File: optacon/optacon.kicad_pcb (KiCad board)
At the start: 2 copper layers, 61.9 x 95.9 mm, 27 parts, among them J1 Conn_01x12, U1 HV528, U2 HV528, U3 DRV2665

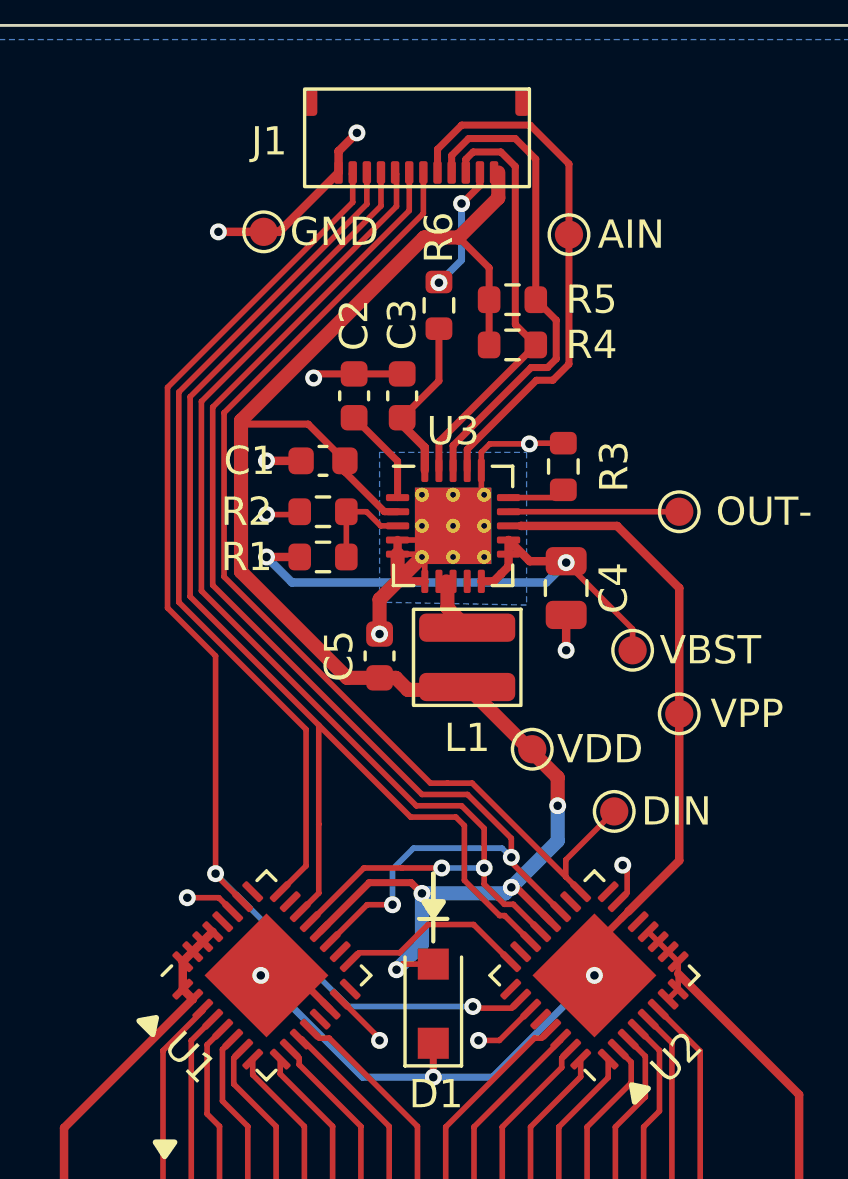
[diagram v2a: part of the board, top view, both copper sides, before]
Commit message: move vias out of pad ; fix ground plane under hv528
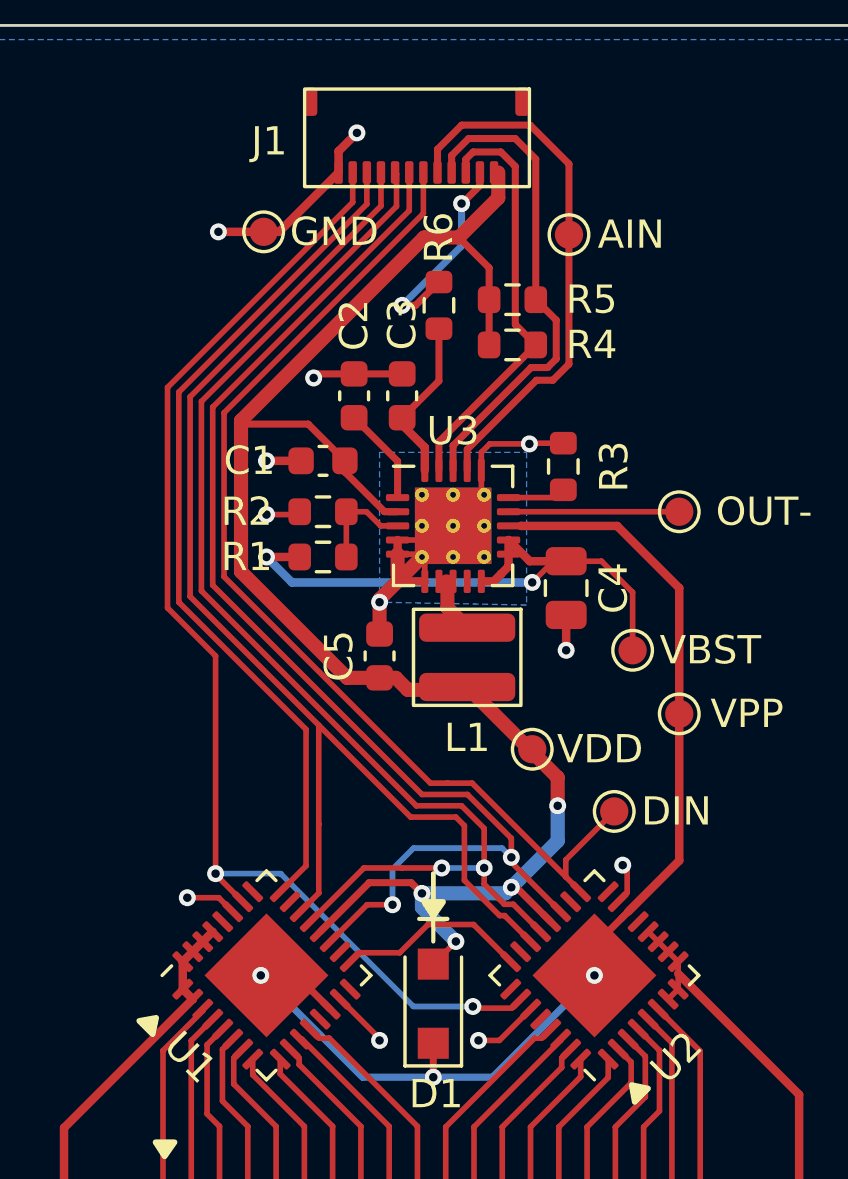
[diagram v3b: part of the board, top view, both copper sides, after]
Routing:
- net /REG: track 4.53 -> 7.49 mm
- net /VDD: track 62.9 -> 61.8 mm
- net /VBST: track 21.0 -> 21.8 mm
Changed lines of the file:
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@@
     )
   )
+  (gr_rect (start 117.4 42.65) (end 90.6 47.75) (layer "B.SilkS") (width 0.15) (fill solid))
   (gr_line (start 103.7 72) (end 104.7 72) (layer "F.SilkS") (width 0.15))
   (gr_poly
@@
   (segment (start 103.3 63.9) (end 105.3 63.9) (width 0.5) (layer "F.Cu") (net 33))
   (segment (start 106.175 50.1) (end 106.175 48.975) (width 0.25) (layer "F.Cu") (net 33))
-  (segment (start 103.098511 73.6) (end 102.9 73.798511) (width 0.2) (layer "F.Cu") (net 33))
   (segment (start 102.3 63.475) (end 102.875 63.475) (width 0.5) (layer "F.Cu") (net 33))
   (segment (start 105.4 63.8) (end 108.6 67) (width 0.5) (layer "F.Cu") (net 33))
@@
   (segment (start 97.4 54.377126) (end 103.877126 47.9) (width 0.5) (layer "F.Cu") (net 33))
   (segment (start 102.477672 57.6) (end 102.9375 57.6) (width 0.25) (layer "F.Cu") (net 33))
+  (segment (start 104.2 73.6) (end 105 72.8) (width 0.2) (layer "F.Cu") (net 33))
   (segment (start 108.353204 72.099651) (end 107.138664 70.885111) (width 0.25) (layer "F.Cu") (net 33))
   (segment (start 106.175 48.975) (end 105.1 47.9) (width 0.25) (layer "F.Cu") (net 33))
@@
   (segment (start 101.075 55.8) (end 99.775 54.5) (width 0.25) (layer "F.Cu") (net 33))
   (segment (start 103.877126 47.9) (end 105.1 47.9) (width 0.5) (layer "F.Cu") (net 33))
-  (segment (start 104.2 73.6) (end 103.098511 73.6) (width 0.2) (layer "F.Cu") (net 33))
   (segment (start 102.3 63.475) (end 101.152126 63.475) (width 0.5) (layer "F.Cu") (net 33))
   (via (at 108.6 68) (size 0.6) (drill 0.3) (layers "F.Cu" "B.Cu") (net 33))
   (via (at 103.8 71.1) (size 0.6) (drill 0.3) (layers "F.Cu" "B.Cu") (net 33))
   (via (at 106.960222 70.884378) (size 0.6) (drill 0.3) (layers "F.Cu" "B.Cu") (net 33))
-  (via (at 102.9 73.798511) (size 0.6) (drill 0.3) (layers "F.Cu" "B.Cu") (net 33))
+  (via (at 105 72.8) (size 0.6) (drill 0.3) (layers "F.Cu" "B.Cu") (net 33))
+  (segment (start 103.8 71.1) (end 103.8 71.6) (width 0.5) (layer "B.Cu") (net 33))
   (segment (start 106.7446 71.1) (end 106.960222 70.884378) (width 0.5) (layer "B.Cu") (net 33))
   (segment (start 103.8 71.1) (end 106.7446 71.1) (width 0.5) (layer "B.Cu") (net 33))
   (segment (start 108.6 68) (end 108.6 69.2446) (width 0.5) (layer "B.Cu") (net 33))
   (segment (start 108.6 69.2446) (end 106.960222 70.884378) (width 0.5) (layer "B.Cu") (net 33))
-  (segment (start 102.9 73.798511) (end 103.8 72.898511) (width 0.5) (layer "B.Cu") (net 33))
-  (segment (start 103.8 72.898511) (end 103.8 71.1) (width 0.5) (layer "B.Cu") (net 33))
+  (segment (start 103.8 71.6) (end 105 72.8) (width 0.5) (layer "B.Cu") (net 33))
   (segment (start 97.460311 71.392544) (end 96.5 70.432233) (width 0.2) (layer "F.Cu") (net 34))
   (segment (start 105.657515 75.157515) (end 105.6 75.1) (width 0.2) (layer "F.Cu") (net 34))
@@
   (segment (start 96.5 62.7) (end 96.5 70.4) (width 0.2) (layer "F.Cu") (net 34))
   (segment (start 107.292544 74.839689) (end 106.974718 75.157515) (width 0.2) (layer "F.Cu") (net 34))
-  (segment (start 101.29952 45.65048) (end 101.35 45.6) (width 0.2) (layer "F.Cu") (net 34))
   (segment (start 106.974718 75.157515) (end 105.657515 75.157515) (width 0.2) (layer "F.Cu") (net 34))
   (via (at 96.5 70.4) (size 0.6) (drill 0.3) (layers "F.Cu" "B.Cu") (net 34))
   (via (at 105.6 75.1) (size 0.6) (drill 0.3) (layers "F.Cu" "B.Cu") (net 34))
-  (segment (start 101.2 75.1) (end 96.5 70.4) (width 0.2) (layer "B.Cu") (net 34))
-  (segment (start 105.6 75.1) (end 101.2 75.1) (width 0.2) (layer "B.Cu") (net 34))
+  (segment (start 98.8 70.4) (end 96.5 70.4) (width 0.2) (layer "B.Cu") (net 34))
+  (segment (start 103.5 75.1) (end 98.8 70.4) (width 0.2) (layer "B.Cu") (net 34))
+  (segment (start 105.6 75.1) (end 103.5 75.1) (width 0.2) (layer "B.Cu") (net 34))
   (segment (start 104.1 67.2) (end 104.7 67.2) (width 0.2) (layer "F.Cu") (net 35))
   (segment (start 104.7 67.2) (end 105.574874 67.2) (width 0.2) (layer "F.Cu") (net 35))
@@
   (segment (start 97.106757 71.746097) (end 96.612673 71.252013) (width 0.2) (layer "F.Cu") (net 40))
   (segment (start 102.9375 59.1) (end 102.9375 59.8375) (width 0.5) (layer "F.Cu") (net 40))
-  (segment (start 99.525 55.9) (end 99.325 56.1) (width 0.3) (layer "F.Cu") (net 40))
   (segment (start 99.475 57.6) (end 99.375 57.7) (width 0.2) (layer "F.Cu") (net 40))
   (segment (start 102.9375 58.6) (end 104.4 58.6) (width 0.2) (layer "F.Cu") (net 40))
@@
   (via (at 96.6 47.7) (size 0.6) (drill 0.3) (layers "F.Cu" "B.Cu") (net 40))
   (via (at 108.9 62.5) (size 0.6) (drill 0.3) (layers "F.Cu" "B.Cu") (net 40))
-  (via (at 102.3 61.925) (size 0.6) (drill 0.3) (layers "F.Cu" "B.Cu") (net 40))
+  (via (at 102.3 60.8) (size 0.6) (drill 0.3) (layers "F.Cu" "B.Cu") (net 40))
   (via (at 110.9 70.1) (size 0.6) (drill 0.3) (layers "F.Cu" "B.Cu") (net 40))
   (via (at 102.3 76.3) (size 0.6) (drill 0.3) (layers "F.Cu" "B.Cu") (net 40))
@@
   (segment (start 109.9 72.93934) (end 109.9 74) (width 0.25) (layer "F.Cu") (net 41))
   (segment (start 110.702151 58.102151) (end 112.9 60.3) (width 0.3) (layer "F.Cu") (net 41))
-  (segment (start 111.093243 71.746097) (end 111.093243 71.706757) (width 0.25) (layer "F.Cu") (net 41))
   (segment (start 109.9 74) (end 109.900002 74) (width 0.25) (layer "F.Cu") (net 41))
   (segment (start 111.093243 71.746097) (end 109.9 72.93934) (width 0.25) (layer "F.Cu") (net 41))
@@
   (segment (start 101.4 54.275) (end 102.9375 55.8125) (width 0.25) (layer "F.Cu") (net 42))
   (segment (start 102.9375 55.8125) (end 102.9375 57.1) (width 0.25) (layer "F.Cu") (net 42))
+  (segment (start 103.575 50.3) (end 104.4 49.475) (width 0.25) (layer "F.Cu") (net 43))
   (segment (start 105.2 46.7) (end 105.215006 46.7) (width 0.25) (layer "F.Cu") (net 43))
-  (segment (start 104.4 49.475) (end 104.4 49.5) (width 0.25) (layer "F.Cu") (net 43))
   (segment (start 105.215006 46.7) (end 105.85 46.065006) (width 0.25) (layer "F.Cu") (net 43))
   (segment (start 105.85 46.065006) (end 105.85 45.6) (width 0.25) (layer "F.Cu") (net 43))
+  (segment (start 103.1 50.3) (end 103.575 50.3) (width 0.25) (layer "F.Cu") (net 43))
   (via (at 105.2 46.7) (size 0.6) (drill 0.3) (layers "F.Cu" "B.Cu") (net 43))
-  (via (at 104.4 49.5) (size 0.6) (drill 0.3) (layers "F.Cu" "B.Cu") (net 43))
-  (segment (start 105.2 46.7) (end 105.2 48.7) (width 0.25) (layer "B.Cu") (net 43))
-  (segment (start 105.2 48.7) (end 104.4 49.5) (width 0.25) (layer "B.Cu") (net 43))
+  (via (at 103.1 50.3) (size 0.6) (drill 0.3) (layers "F.Cu" "B.Cu") (net 43))
+  (segment (start 105.2 46.7) (end 105.2 48.2) (width 0.25) (layer "B.Cu") (net 43))
+  (segment (start 105.2 48.2) (end 103.1 50.3) (width 0.25) (layer "B.Cu") (net 43))
   (segment (start 103.1 54.525) (end 103.9 55.325) (width 0.3) (layer "F.Cu") (net 44))
   (segment (start 104.4 52.975) (end 104.4 51.125) (width 0.25) (layer "F.Cu") (net 44))
@@
   (segment (start 106.8625 57.1) (end 108.525 57.1) (width 0.2) (layer "F.Cu") (net 51))
   (segment (start 108.525 57.1) (end 108.8 56.825) (width 0.2) (layer "F.Cu") (net 51))
-  (segment (start 108.9 59.4) (end 111.25 61.75) (width 0.2) (layer "F.Cu") (net 53))
   (segment (start 106.599511 59.799511) (end 106.336522 60.0625) (width 0.3) (layer "F.Cu") (net 53))
   (segment (start 106.336522 60.0625) (end 105.9 60.0625) (width 0.3) (layer "F.Cu") (net 53))
-  (segment (start 111.25 61.75) (end 111.25 62.5) (width 0.2) (layer "F.Cu") (net 53))
+  (segment (start 110.15 59.35) (end 108.45 59.35) (width 0.2) (layer "F.Cu") (net 53))
+  (segment (start 111.25 62.5) (end 111.25 60.45) (width 0.2) (layer "F.Cu") (net 53))
   (segment (start 107.6125 59.35) (end 106.8625 58.6) (width 0.3) (layer "F.Cu") (net 53))
   (segment (start 106.8625 58.6) (end 106.8625 59.1) (width 0.3) (layer "F.Cu") (net 53))
+  (segment (start 111.25 60.45) (end 110.15 59.35) (width 0.2) (layer "F.Cu") (net 53))
   (segment (start 98.3 59.2) (end 99.475 59.2) (width 0.3) (layer "F.Cu") (net 53))
   (segment (start 108.9 59.35) (end 107.6125 59.35) (width 0.3) (layer "F.Cu") (net 53))
   (segment (start 106.8625 59.536522) (end 106.599511 59.799511) (width 0.3) (layer "F.Cu") (net 53))
   (segment (start 106.8625 59.1) (end 106.8625 59.536522) (width 0.3) (layer "F.Cu") (net 53))
-  (via (at 108.9 59.4) (size 0.6) (drill 0.3) (layers "F.Cu" "B.Cu") (net 53))
+  (segment (start 108.45 59.35) (end 107.7 60.1) (width 0.2) (layer "F.Cu") (net 53))
+  (via (at 107.7 60.1) (size 0.6) (drill 0.3) (layers "F.Cu" "B.Cu") (net 53))
   (via (at 98.3 59.2) (size 0.6) (drill 0.3) (layers "F.Cu" "B.Cu") (net 53))
-  (segment (start 108.9 59.4) (end 108.2 60.1) (width 0.3) (layer "B.Cu") (net 53))
-  (segment (start 99.2 60.1) (end 98.3 59.2) (width 0.3) (layer "B.Cu") (net 53))
-  (segment (start 108.2 60.1) (end 99.2 60.1) (width 0.3) (layer "B.Cu") (net 53))
+  (segment (start 98.3 59.2) (end 99.2 60.1) (width 0.3) (layer "B.Cu") (net 53))
+  (segment (start 99.2 60.1) (end 107.7 60.1) (width 0.3) (layer "B.Cu") (net 53))
   (segment (start 106.8625 57.6) (end 112.9 57.6) (width 0.2) (layer "F.Cu") (net 54))
   (segment (start 105.625126 72.2) (end 106.93899 73.513864) (width 0.2) (layer "F.Cu") (net 55))

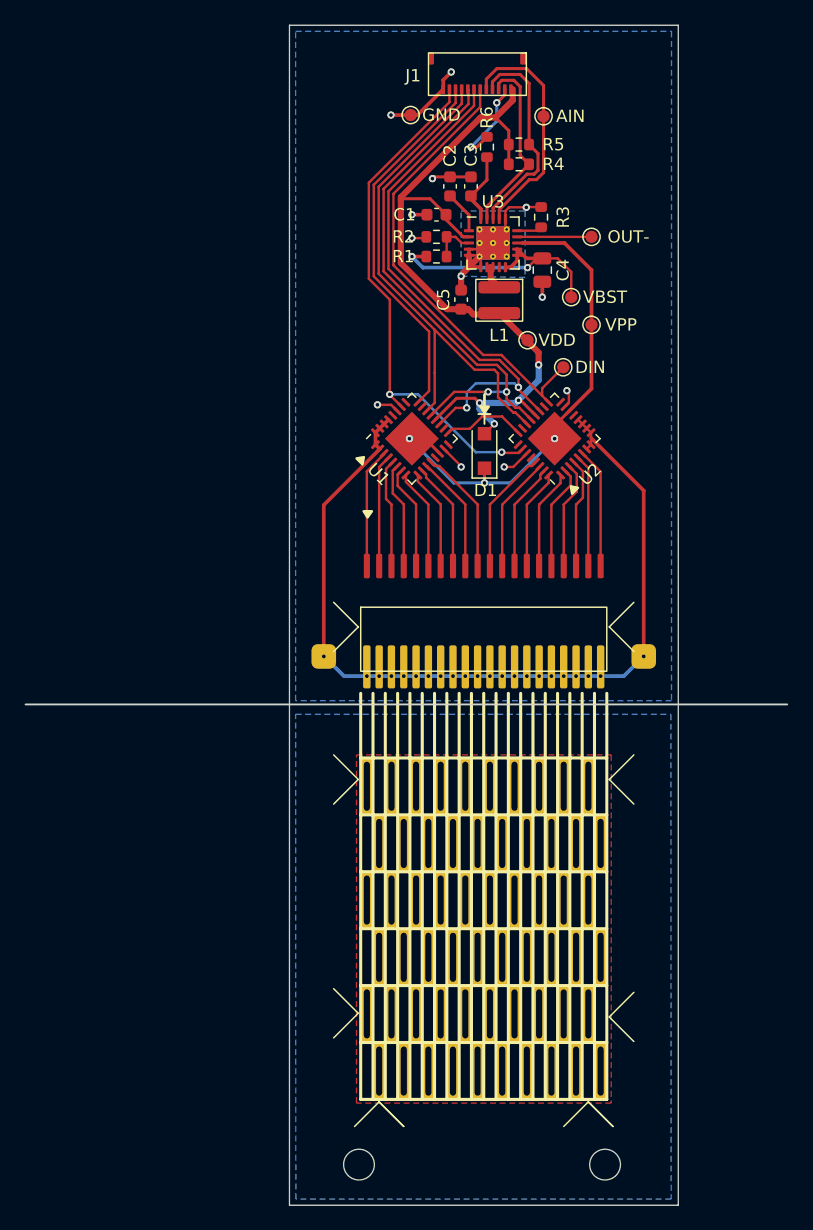
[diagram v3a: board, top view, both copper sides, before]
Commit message: thermal vias for HV509/HV528
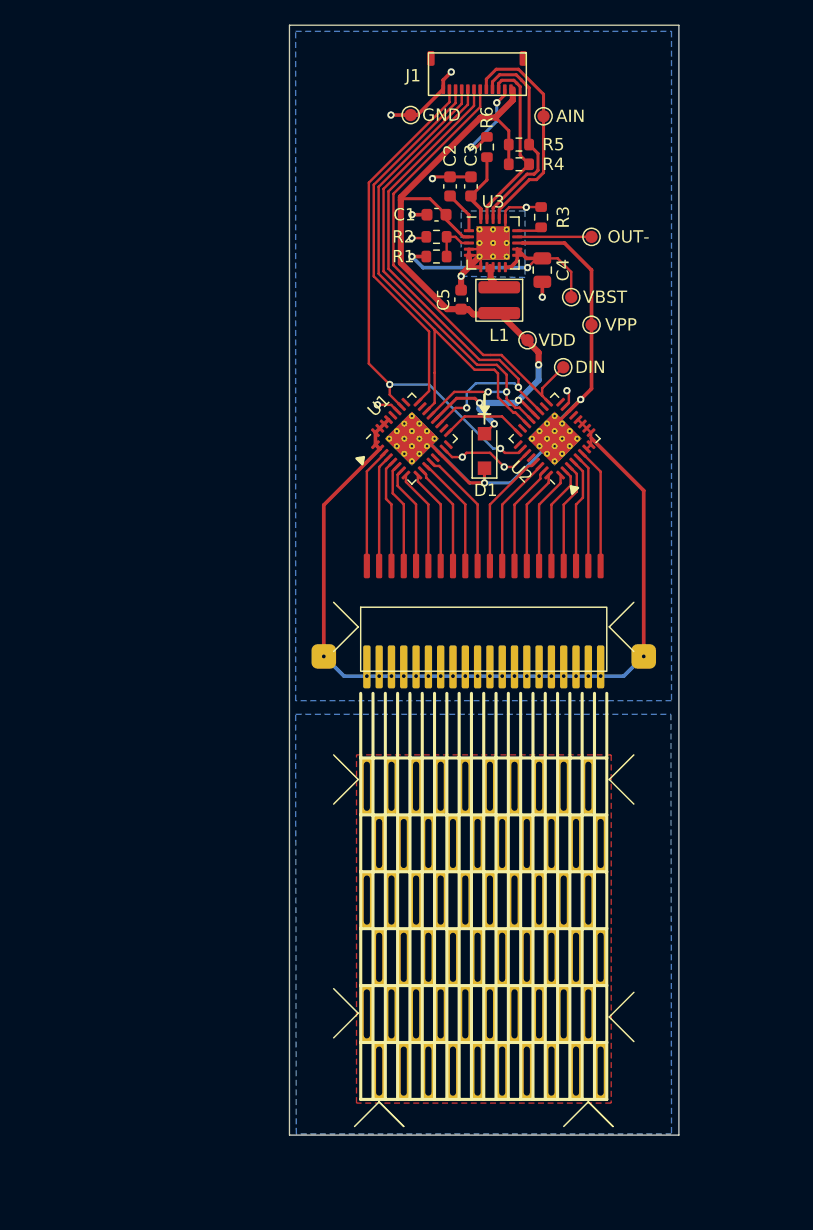
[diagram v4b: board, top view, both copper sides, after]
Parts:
- removed REF** (x2): MountingHole_2.5mm, MountingHole:MountingHole_2.5mm
- U1, U2: footprint Package_DFN_QFN:HVQFN-32-1EP_5x5mm_P0.5mm_EP3.1x3.1mm -> Package_DFN_QFN:HVQFN-32-1EP_5x5mm_P0.5mm_EP3.1x3.1mm_ThermalVias
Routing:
- net /VPP: track 40.4 -> 48.0 mm, vias 3 -> 2
- net GND: track 35.3 -> 39.1 mm
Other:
- board size 61.9 x 95.9 mm -> 31.7 x 90.2 mm

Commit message: test points
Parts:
- added TP10: TestPoint, TestPoint:TestPoint_Pad_D1.0mm, F.Cu at (111.5, 48.8)
- added TP11: TestPoint, TestPoint:TestPoint_Pad_D1.0mm, F.Cu at (111.5, 44.5)
- added TP12: TestPoint, TestPoint:TestPoint_Pad_D1.0mm, F.Cu at (91.7, 44.6)
- added TP13: TestPoint, TestPoint:TestPoint_Pad_D1.0mm, F.Cu at (91.7, 46.7)
- added TP14: TestPoint, TestPoint:TestPoint_Pad_D1.0mm, F.Cu at (91.7, 48.8)
- added TP15: TestPoint, TestPoint:TestPoint_Pad_D1.0mm, F.Cu at (91.7, 53.0)
- added TP2: TestPoint, TestPoint:TestPoint_Pad_D1.0mm, F.Cu at (91.7, 55.2)
- added TP2: TestPoint, TestPoint:TestPoint_Pad_D1.0mm, F.Cu at (111.5, 50.9)
- added TP8: TestPoint, TestPoint:TestPoint_Pad_D1.0mm, F.Cu at (91.7, 50.9)
- added TP9: TestPoint, TestPoint:TestPoint_Pad_D1.0mm, F.Cu at (111.5, 46.6)
- moved TP7 32.0 mm to (91.6, 42.5)
- moved TP2 25.0 mm to (111.3, 69.0)
- moved TP6 5.91 mm to (111.5, 42.5)
- moved TP1 3.69 mm to (111.3, 66.8)
- moved TP3 1.60 mm to (111.3, 64.7)
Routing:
- net /CLK: track 43.7 -> 58.5 mm
- net /LE: track 42.9 -> 56.2 mm
- net /POL: track 42.7 -> 56.0 mm
- net /DOUT: track 30.4 -> 43.6 mm
- net /DIN: track 37.5 -> 49.3 mm
- net /REG: track 7.49 -> 15.0 mm, vias 2 -> 3
- net /AIN: track 18.6 -> 23.6 mm
- net /SDA: track 15.0 -> 19.7 mm, vias 0 -> 2
- net GND: track 39.1 -> 35.3 mm, vias 12 -> 13
- net /SCL: track 17.1 -> 20.7 mm, vias 0 -> 2
- net /VBIAS: track 42.8 -> 46.1 mm
- net /VDD: track 61.8 -> 64.5 mm
